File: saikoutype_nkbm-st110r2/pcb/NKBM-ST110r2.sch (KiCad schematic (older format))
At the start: 28 parts

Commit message: Begin conversion to 最悪ゴミ
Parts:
- removed L06, L07, L08, L09: LED, symbol LED
- removed MCU1: Teesny2.0++, null_keyboard:TEENSY2.0++, symbol Teesny2.0++
- removed R06, R07, R08, R09: 330, symbol R
- added H?: EXPANSION, symbol NKBM-ST110r2-rescue:SERIAL_HEADER
- added H?: SPI, symbol NKBM-ST110r2-rescue:SPI_HEADER
- added H?: RESET, symbol NKBM-ST110r2-rescue:RST_HEADER
- added H?: VCCIN, symbol NKBM-ST110r2-rescue:VCCIN_HEADER
- added H?: USB_BREAKOUT, symbol NKBM-ST110r2-rescue:USB_BREAKOUT
- added J? (x3): 2012670005, MOLEX_2012670005, symbol Molex_USB-C:2012670005
- added L? (x10): LED, symbol Device:LED
- added MCU?: Teesny2.0++, null_keyboard:TEENSY2.0++, symbol NKBM-ST110r2-rescue:Teesny2.0++
- added P?: USB_MINI_B, symbol NKBM-ST110r2-rescue:USB_OTG
- added R? (x10): 330, symbol Device:R
- added U1: AT90USB1286-AU, eec:Microchip___Atmel-AT90USB1286-AU-Level_A, symbol MCU_Microchip_AVR:AT90USB1286-AU
- added U?: TUSB8041, Package_DFN_QFN:QFN-64-1EP_9x9mm_P0.5mm_EP6x6mm_ThermalVias, symbol Interface_USB:TUSB8041
- added USB_POWER?: SOLDER_JUMPER, SOLDER_BRIDGE, symbol NKBM-ST110r2-rescue:GS2
- H1: renamed from H?; symbol USB_BREAKOUT -> NKBM-ST110r2-rescue:USB_BREAKOUT
- H11: symbol SPI_HEADER -> NKBM-ST110r2-rescue:SPI_HEADER
- H21: symbol SERIAL_HEADER -> NKBM-ST110r2-rescue:SERIAL_HEADER
- H31: symbol RST_HEADER -> NKBM-ST110r2-rescue:RST_HEADER
- H41: symbol VCCIN_HEADER -> NKBM-ST110r2-rescue:VCCIN_HEADER
- L0: renamed from L00; symbol LED -> Device:LED
- L1: renamed from L01; symbol LED -> Device:LED
- L2: renamed from L02; symbol LED -> Device:LED
- L3: renamed from L03; symbol LED -> Device:LED
- L4: renamed from L04; symbol LED -> Device:LED
- L5: renamed from L05; symbol LED -> Device:LED
- P1: renamed from P?; symbol USB_OTG -> NKBM-ST110r2-rescue:USB_OTG
- R0: renamed from R00; symbol R -> Device:R
- R1: renamed from R01; symbol R -> Device:R
- R2: renamed from R02; symbol R -> Device:R
- R3: renamed from R03; symbol R -> Device:R
- R4: renamed from R04; symbol R -> Device:R
- R5: renamed from R05; symbol R -> Device:R
- USB_POWER1: renamed from USB_POWER; symbol GS2 -> NKBM-ST110r2-rescue:GS2
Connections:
- net labels added: ROT_A, ROT_B, ROT_SWITCH
- wire segments 129 -> 241
- no-connect marks 6 -> 7
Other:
- moved on the sheet: USB_POWER1

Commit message: Add Net Labels
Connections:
- net labels added: DM_UP, DP_UP, SSRXM_UP, SSRXP_UP, SSTXM_UP, SSTXP_UP
- wire segments 241 -> 272
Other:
- moved on the sheet: J?
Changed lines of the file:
@@
 L Molex_USB-C:2012670005 J?
 U 1 1 607F43D1
-P 11900 7600
-F 0 "J?" H 11900 8567 50  0000 C CNN
-F 1 "2012670005" H 11900 8476 50  0000 C CNN
-F 2 "MOLEX_2012670005" H 11900 7600 50  0001 L BNN
-F 3 "" H 11900 7600 50  0001 L BNN
-F 4 "3.86mm" H 11900 7600 50  0001 L BNN "MAXIMUM_PACKAGE_HEIGHT"
-F 5 "C" H 11900 7600 50  0001 L BNN "PARTREV"
-F 6 "Molex" H 11900 7600 50  0001 L BNN "MANUFACTURER"
-F 7 "Manufacturer Recommendation" H 11900 7600 50  0001 L BNN "STANDARD"
-	1    11900 7600
+P 12100 7650
+F 0 "J?" H 12100 8617 50  0000 C CNN
+F 1 "2012670005" H 12100 8526 50  0000 C CNN
+F 2 "MOLEX_2012670005" H 12100 7650 50  0001 L BNN
+F 3 "" H 12100 7650 50  0001 L BNN
+F 4 "3.86mm" H 12100 7650 50  0001 L BNN "MAXIMUM_PACKAGE_HEIGHT"
+F 5 "C" H 12100 7650 50  0001 L BNN "PARTREV"
+F 6 "Molex" H 12100 7650 50  0001 L BNN "MANUFACTURER"
+F 7 "Manufacturer Recommendation" H 12100 7650 50  0001 L BNN "STANDARD"
+	1    12100 7650
 	1    0    0    -1
 $EndComp
@@
 L Molex_USB-C:2012670005 J?
 U 1 1 6077E66D
-P 14350 1550
-F 0 "J?" H 14350 2517 50  0000 C CNN
-F 1 "2012670005" H 14350 2426 50  0000 C CNN
-F 2 "MOLEX_2012670005" H 14350 1550 50  0001 L BNN
-F 3 "" H 14350 1550 50  0001 L BNN
-F 4 "3.86mm" H 14350 1550 50  0001 L BNN "MAXIMUM_PACKAGE_HEIGHT"
-F 5 "C" H 14350 1550 50  0001 L BNN "PARTREV"
-F 6 "Molex" H 14350 1550 50  0001 L BNN "MANUFACTURER"
-F 7 "Manufacturer Recommendation" H 14350 1550 50  0001 L BNN "STANDARD"
-	1    14350 1550
+P 13250 1500
+F 0 "J?" H 13250 2467 50  0000 C CNN
+F 1 "2012670005" H 13250 2376 50  0000 C CNN
+F 2 "MOLEX_2012670005" H 13250 1500 50  0001 L BNN
+F 3 "" H 13250 1500 50  0001 L BNN
+F 4 "3.86mm" H 13250 1500 50  0001 L BNN "MAXIMUM_PACKAGE_HEIGHT"
+F 5 "C" H 13250 1500 50  0001 L BNN "PARTREV"
+F 6 "Molex" H 13250 1500 50  0001 L BNN "MANUFACTURER"
+F 7 "Manufacturer Recommendation" H 13250 1500 50  0001 L BNN "STANDARD"
+	1    13250 1500
 	-1   0    0    1
 $EndComp
@@
 L Molex_USB-C:2012670005 J?
 U 1 1 6073AD09
-P 12300 1550
-F 0 "J?" H 12300 2517 50  0000 C CNN
-F 1 "2012670005" H 12300 2426 50  0000 C CNN
-F 2 "MOLEX_2012670005" H 12300 1550 50  0001 L BNN
-F 3 "" H 12300 1550 50  0001 L BNN
-F 4 "3.86mm" H 12300 1550 50  0001 L BNN "MAXIMUM_PACKAGE_HEIGHT"
-F 5 "C" H 12300 1550 50  0001 L BNN "PARTREV"
-F 6 "Molex" H 12300 1550 50  0001 L BNN "MANUFACTURER"
-F 7 "Manufacturer Recommendation" H 12300 1550 50  0001 L BNN "STANDARD"
-	1    12300 1550
+P 11650 1450
+F 0 "J?" H 11650 2417 50  0000 C CNN
+F 1 "2012670005" H 11650 2326 50  0000 C CNN
+F 2 "MOLEX_2012670005" H 11650 1450 50  0001 L BNN
+F 3 "" H 11650 1450 50  0001 L BNN
+F 4 "3.86mm" H 11650 1450 50  0001 L BNN "MAXIMUM_PACKAGE_HEIGHT"
+F 5 "C" H 11650 1450 50  0001 L BNN "PARTREV"
+F 6 "Molex" H 11650 1450 50  0001 L BNN "MANUFACTURER"
+F 7 "Manufacturer Recommendation" H 11650 1450 50  0001 L BNN "STANDARD"
+	1    11650 1450
 	-1   0    0    1
 $EndComp
@@
 	5400 6900 5400 8150
 Connection ~ 5800 6600
+Wire Wire Line
+	11400 6950 10800 6950
+Wire Wire Line
+	11400 7050 10800 7050
+Wire Wire Line
+	11400 7150 10800 7150
+Wire Wire Line
+	11400 7250 10800 7250
+Wire Wire Line
+	11400 7350 10800 7350
+Wire Wire Line
+	11400 7450 10800 7450
+Wire Wire Line
+	11400 7650 10800 7650
+Wire Wire Line
+	11400 7750 10800 7750
+Wire Wire Line
+	11400 7850 10800 7850
+Wire Wire Line
+	11400 7950 10800 7950
+Wire Wire Line
+	11400 8050 10800 8050
+Wire Wire Line
+	11400 8150 10800 8150
+Wire Wire Line
+	12800 6950 12800 7050
+Connection ~ 12800 7050
+Wire Wire Line
+	12800 7050 12800 7150
+Connection ~ 12800 7150
+Wire Wire Line
+	12800 7150 12800 7250
+Wire Wire Line
+	12800 7050 13400 7050
+Wire Wire Line
+	12800 7950 12800 8050
+Connection ~ 12800 8050
+Wire Wire Line
+	12800 8050 12800 8150
+Connection ~ 12800 8150
+Wire Wire Line
+	12800 8150 12800 8250
+Connection ~ 12800 8250
+Wire Wire Line
+	12800 8250 12800 8350
+Wire Wire Line
+	12800 8150 13400 8150
+Wire Wire Line
+	12800 7450 13100 7450
+Wire Wire Line
+	12800 7650 13100 7650
+Wire Wire Line
+	12800 7550 13100 7550
+Wire Wire Line
+	12800 7750 13100 7750
+Text Label 13100 7450 0    60   ~ 0
+DP_UP
+Text Label 13100 7650 0    60   ~ 0
+DP_UP
+Text Label 13100 7550 0    60   ~ 0
+DM_UP
+Text Label 13100 7750 0    60   ~ 0
+DM_UP
+Wire Wire Line
+	12200 5800 12200 6000
+Wire Wire Line
+	11900 5800 11900 6300
+Wire Wire Line
+	11800 5800 11800 6400
+Wire Wire Line
+	11700 5800 11700 6500
+Text Label 12200 6000 0    60   ~ 0
+DM_UP
+Wire Wire Line
+	12100 5800 12100 6100
+Text Label 12100 6100 0    60   ~ 0
+DP_UP
+Wire Wire Line
+	12000 5800 12000 6200
+Text Label 12000 6200 0    60   ~ 0
+SSRXM_UP
+Text Label 11900 6300 0    60   ~ 0
+SSRXP_UP
+Text Label 11800 6400 0    60   ~ 0
+SSTXM_UP
+Text Label 11700 6500 0    60   ~ 0
+SSTXP_UP
 Wire Bus Line
 	26550 550  26550 1950
@@
 	5850 3700 5850 4400
 Wire Bus Line
+	5400 6125 5400 6900
+Wire Bus Line
+	8150 2700 8150 6600
+Wire Bus Line
 	32900 -75  32900 1950
 Wire Bus Line
@@
 	29750 -1900 29750 1950
 Wire Bus Line
-	5400 6125 5400 6900
-Wire Bus Line
-	8150 2700 8150 6600
-Wire Bus Line
 	30750 -75  30750 1950
 Wire Bus Line
@@
 Wire Bus Line
 	3250 6125 3250 8150
+Text Label 10800 6950 0    60   ~ 0
+SSTXP_UP
+Text Label 10800 7150 0    60   ~ 0
+SSTXP_UP
+Text Label 10800 7050 0    60   ~ 0
+SSTXM_UP
+Text Label 10800 7250 0    60   ~ 0
+SSTXM_UP
+Text Label 10800 7850 0    60   ~ 0
+SSRXP_UP
+Text Label 10800 7950 0    60   ~ 0
+SSRXM_UP
+Text Label 10800 8050 0    60   ~ 0
+SSRXP_UP
+Text Label 10800 8150 0    60   ~ 0
+SSRXM_UP
 $EndSCHEMATC

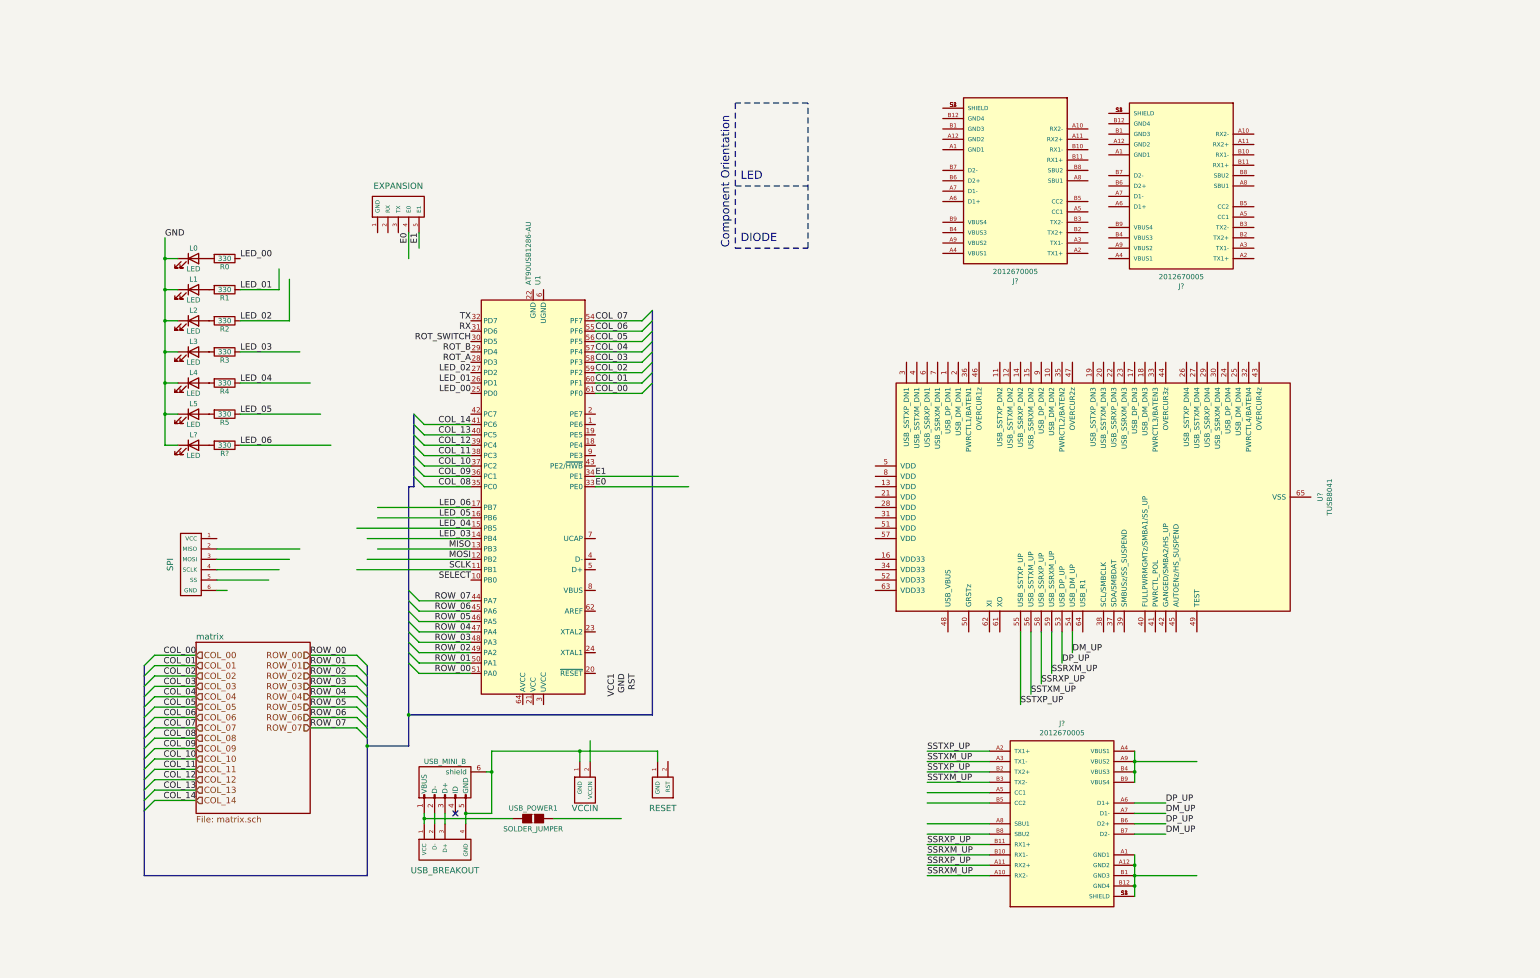
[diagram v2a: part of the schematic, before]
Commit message: Initial rotary. Build out all USB lanes
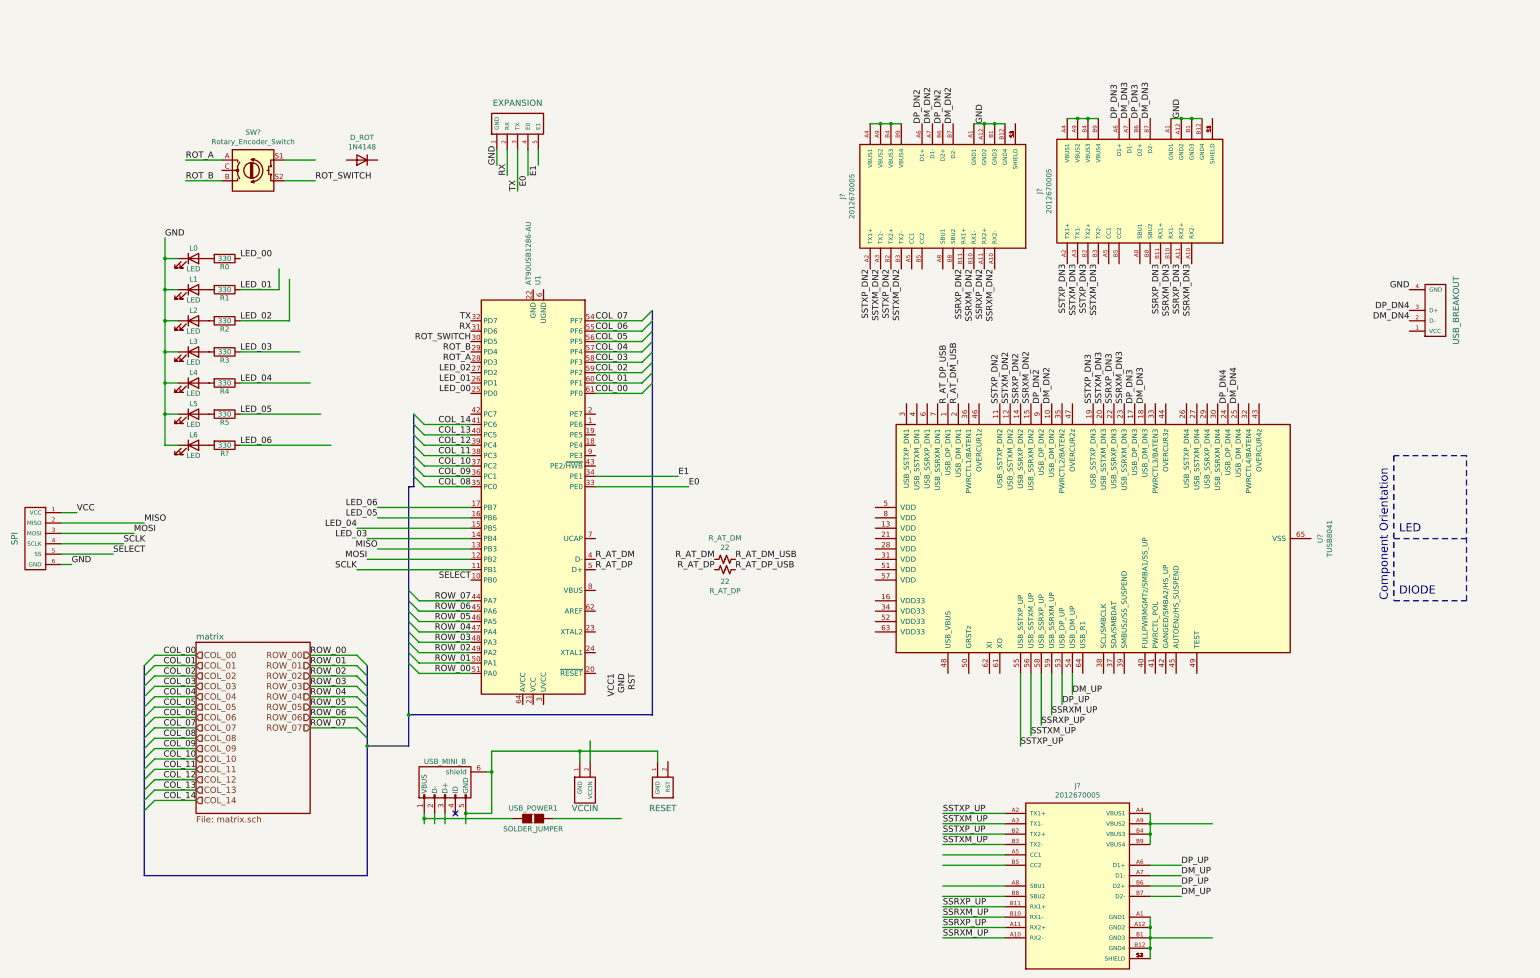
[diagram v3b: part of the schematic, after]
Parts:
- added D_ROT: 1N4148, Diode_THT:D_DO-35_SOD27_P7.62mm_Horizontal, symbol Diode:1N4148
- added R_AT_DM, R_AT_DP: 22, symbol Device:R_Small_US
- added SW?: Rotary_Encoder_Switch, symbol Device:Rotary_Encoder_Switch
- gave numbers to parts that had none: 1
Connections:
- net labels added: DM_DN2, DM_DN3, DM_DN4, DP_DN2, DP_DN3, DP_DN4, R_AT_DM, R_AT_DM_USB, R_AT_DP, R_AT_DP_USB, SSRXM_DN2, SSRXM_DN3, SSRXP_DN2, SSRXP_DN3, SSTXM_DN2, SSTXM_DN3, SSTXP_DN2, SSTXP_DN3
- wire segments 272 -> 292
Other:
- moved on the sheet: J?, U?
